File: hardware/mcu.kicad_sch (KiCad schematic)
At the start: 11 parts, among them J12 PICO UTIL, U1 Pico 2

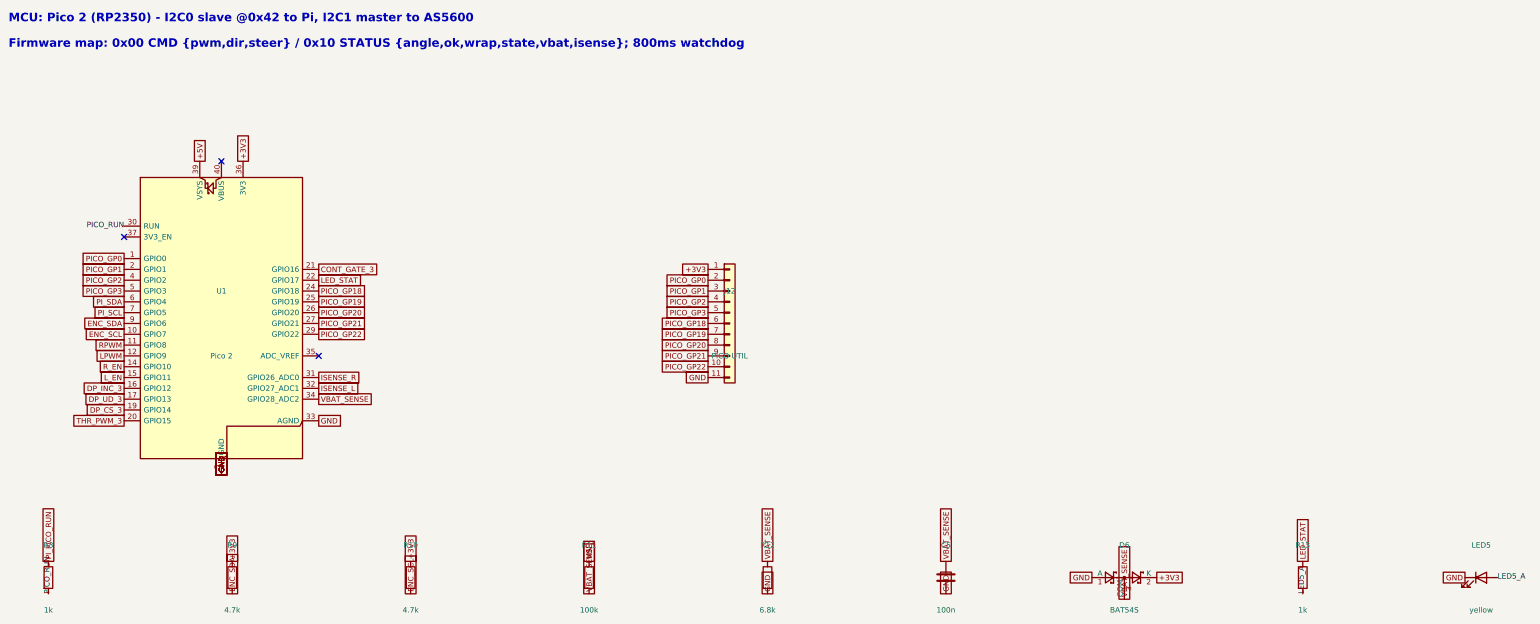
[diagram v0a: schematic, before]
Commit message: feat: custom footprints (Pololu buck, Pico+SWD), Pi-reflashable Pico via SWD on GPIO24/25
Co-Authored-By: Claude Fable 5 <noreply@anthropic.com>
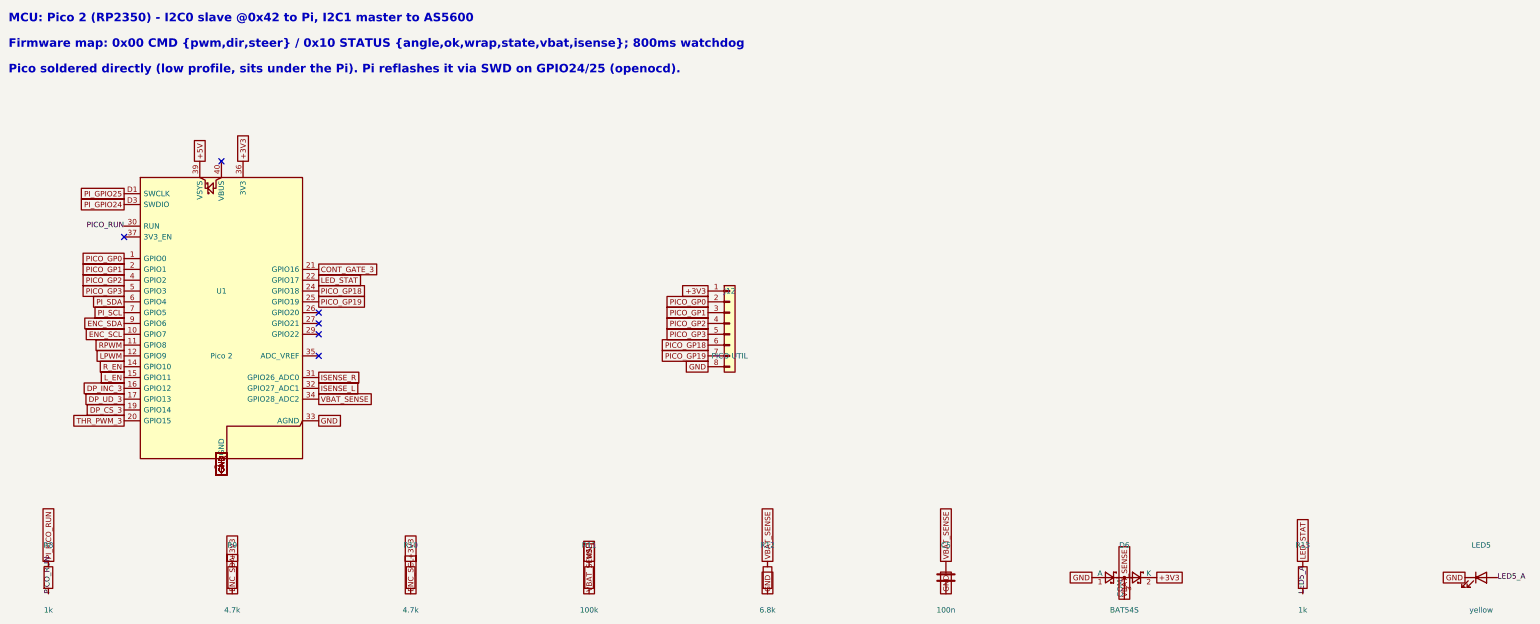
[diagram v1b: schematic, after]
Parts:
- J12: footprint Connector_PinHeader_2.54mm:PinHeader_1x11_P2.54mm_Vertical -> Connector_PinHeader_2.54mm:PinHeader_1x08_P2.54mm_Vertical; symbol Connector_Generic:Conn_01x11 -> Connector_Generic:Conn_01x08
- U1: footprint Module:RaspberryPi_Pico_Common_THT -> vanchor-helm:RaspberryPi_Pico_TH_SWD; symbol MCU_Module:RaspberryPi_Pico -> MCU_Module:RaspberryPi_Pico_Debug
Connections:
- net GND: now also J12.8 (Pin_8), U1.D2 (GND); no longer J12.11 (Pin_11)
- net PICO_GP20: no longer names the net of U1.26 (GPIO20)
- net PICO_GP20: no longer J12.8 (Pin_8)
- net PICO_GP21: no longer names the net of U1.27 (GPIO21)
- net PICO_GP21: no longer J12.9 (Pin_9)
- net PICO_GP22: no longer names the net of U1.29 (GPIO22)
- net PICO_GP22: no longer J12.10 (Pin_10)
- new net PI_GPIO24: U1.D3 (SWDIO)
- new net PI_GPIO25: U1.D1 (SWCLK)
- no-connect marks 3 -> 6
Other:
- note added: "Pico soldered directly (low profile, sits under the Pi). Pi reflashes it via SWD on GPIO24/25 (openocd)."
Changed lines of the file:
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@@
     (effects (font (size 2 2) (bold yes)) (justify left bottom))
   )
-  (symbol (lib_id "MCU_Module:RaspberryPi_Pico") (at 80.01 110.49 0) (unit 1)
+  (text "Pico soldered directly (low profile, sits under the Pi). Pi reflashes it via SWD on GPIO24/25 (openocd)." (exclude_from_sim no) (at 30 52 0)
+    (effects (font (size 2 2) (bold yes)) (justify left bottom))
+  )
+  (symbol (lib_id "MCU_Module:RaspberryPi_Pico_Debug") (at 80.01 110.49 0) (unit 1)
     (exclude_from_sim no) (in_bom yes) (on_board yes) (dnp no)
     (property "Reference" "U1" (at 80.01 102.87 0)
@@
     (property "Value" "Pico 2" (at 80.01 118.11 0)
       (effects (font (size 1.27 1.27))))
-    (property "Footprint" "Module:RaspberryPi_Pico_Common_THT" (at 80.01 110.49 0)
+    (property "Footprint" "vanchor-helm:RaspberryPi_Pico_TH_SWD" (at 80.01 110.49 0)
       (effects (font (size 1.27 1.27)) (hide yes)))
     (property "Datasheet" "" (at 80.01 110.49 0)
@@
     (pin "8")
     (pin "9")
+    (pin "D1")
+    (pin "D2")
+    (pin "D3")
     (instances (project "vanchor-helm" (path "/a0000000-0000-4000-8000-000000000001/c0000000-0000-4000-8000-000000000004" (reference "U1") (unit 1))))
   )
@@
     (instances (project "vanchor-helm" (path "/a0000000-0000-4000-8000-000000000001/c0000000-0000-4000-8000-000000000004" (reference "LED5") (unit 1))))
   )
-  (symbol (lib_id "Connector_Generic:Conn_01x11") (at 199.39 110.49 0) (unit 1)
+  (symbol (lib_id "Connector_Generic:Conn_01x08") (at 199.39 110.49 0) (unit 1)
     (exclude_from_sim no) (in_bom yes) (on_board yes) (dnp no)
     (property "Reference" "J12" (at 199.39 102.87 0)
@@
     (property "Value" "PICO UTIL" (at 199.39 118.11 0)
       (effects (font (size 1.27 1.27))))
-    (property "Footprint" "Connector_PinHeader_2.54mm:PinHeader_1x11_P2.54mm_Vertical" (at 199.39 110.49 0)
+    (property "Footprint" "Connector_PinHeader_2.54mm:PinHeader_1x08_P2.54mm_Vertical" (at 199.39 110.49 0)
       (effects (font (size 1.27 1.27)) (hide yes)))
     (property "Datasheet" "" (at 199.39 110.49 0)
       (effects (font (size 1.27 1.27)) (hide yes)))
     (pin "1")
-    (pin "10")
-    (pin "11")
     (pin "2")
     (pin "3")
@@
     (pin "7")
     (pin "8")
-    (pin "9")
     (instances (project "vanchor-helm" (path "/a0000000-0000-4000-8000-000000000001/c0000000-0000-4000-8000-000000000004" (reference "J12") (unit 1))))
   )
@@
       (effects (font (size 1.27 1.27)) (hide yes)))
   )
-  (global_label "PICO_GP20" (shape passive) (at 102.87 107.95 0.0) (fields_autoplaced yes)
-    (effects (font (size 1.27 1.27)) (justify left))
-    (property "Intersheetrefs" "${INTERSHEET_REFS}" (at 102.87 107.95 0)
-      (effects (font (size 1.27 1.27)) (hide yes)))
-  )
-  (global_label "PICO_GP21" (shape passive) (at 102.87 110.49 0.0) (fields_autoplaced yes)
-    (effects (font (size 1.27 1.27)) (justify left))
-    (property "Intersheetrefs" "${INTERSHEET_REFS}" (at 102.87 110.49 0)
-      (effects (font (size 1.27 1.27)) (hide yes)))
-  )
-  (global_label "GND" (shape passive) (at 80.01 146.05 270.0) (fields_autoplaced yes)
-    (effects (font (size 1.27 1.27)) (justify left))
-    (property "Intersheetrefs" "${INTERSHEET_REFS}" (at 80.01 146.05 0)
-      (effects (font (size 1.27 1.27)) (hide yes)))
-  )
-  (global_label "PICO_GP22" (shape passive) (at 102.87 113.03 0.0) (fields_autoplaced yes)
-    (effects (font (size 1.27 1.27)) (justify left))
-    (property "Intersheetrefs" "${INTERSHEET_REFS}" (at 102.87 113.03 0)
+  (global_label "GND" (shape passive) (at 80.01 146.05 270.0) (fields_autoplaced yes)
+    (effects (font (size 1.27 1.27)) (justify left))
+    (property "Intersheetrefs" "${INTERSHEET_REFS}" (at 80.01 146.05 0)
       (effects (font (size 1.27 1.27)) (hide yes)))
   )
@@
       (effects (font (size 1.27 1.27)) (hide yes)))
   )
+  (global_label "PI_GPIO25" (shape passive) (at 57.15 80.01 180.0) (fields_autoplaced yes)
+    (effects (font (size 1.27 1.27)) (justify right))
+    (property "Intersheetrefs" "${INTERSHEET_REFS}" (at 57.15 80.01 0)
+      (effects (font (size 1.27 1.27)) (hide yes)))
+  )
+  (global_label "GND" (shape passive) (at 80.01 146.05 270.0) (fields_autoplaced yes)
+    (effects (font (size 1.27 1.27)) (justify left))
+    (property "Intersheetrefs" "${INTERSHEET_REFS}" (at 80.01 146.05 0)
+      (effects (font (size 1.27 1.27)) (hide yes)))
+  )
+  (global_label "PI_GPIO24" (shape passive) (at 57.15 82.55 180.0) (fields_autoplaced yes)
+    (effects (font (size 1.27 1.27)) (justify right))
+    (property "Intersheetrefs" "${INTERSHEET_REFS}" (at 57.15 82.55 0)
+      (effects (font (size 1.27 1.27)) (hide yes)))
+  )
   (global_label "PI_PICO_RUN" (shape passive) (at 39.37 166.37 90.0) (fields_autoplaced yes)
     (effects (font (size 1.27 1.27)) (justify left))
@@
       (effects (font (size 1.27 1.27)) (hide yes)))
   )
-  (global_label "+3V3" (shape passive) (at 194.31 97.79 180.0) (fields_autoplaced yes)
-    (effects (font (size 1.27 1.27)) (justify right))
-    (property "Intersheetrefs" "${INTERSHEET_REFS}" (at 194.31 97.79 0)
-      (effects (font (size 1.27 1.27)) (hide yes)))
-  )
-  (global_label "PICO_GP0" (shape passive) (at 194.31 100.33 180.0) (fields_autoplaced yes)
-    (effects (font (size 1.27 1.27)) (justify right))
-    (property "Intersheetrefs" "${INTERSHEET_REFS}" (at 194.31 100.33 0)
-      (effects (font (size 1.27 1.27)) (hide yes)))
-  )
-  (global_label "PICO_GP1" (shape passive) (at 194.31 102.87 180.0) (fields_autoplaced yes)
+  (global_label "+3V3" (shape passive) (at 194.31 102.87 180.0) (fields_autoplaced yes)
     (effects (font (size 1.27 1.27)) (justify right))
     (property "Intersheetrefs" "${INTERSHEET_REFS}" (at 194.31 102.87 0)
       (effects (font (size 1.27 1.27)) (hide yes)))
   )
-  (global_label "PICO_GP2" (shape passive) (at 194.31 105.41 180.0) (fields_autoplaced yes)
+  (global_label "PICO_GP0" (shape passive) (at 194.31 105.41 180.0) (fields_autoplaced yes)
     (effects (font (size 1.27 1.27)) (justify right))
     (property "Intersheetrefs" "${INTERSHEET_REFS}" (at 194.31 105.41 0)
       (effects (font (size 1.27 1.27)) (hide yes)))
   )
-  (global_label "PICO_GP3" (shape passive) (at 194.31 107.95 180.0) (fields_autoplaced yes)
+  (global_label "PICO_GP1" (shape passive) (at 194.31 107.95 180.0) (fields_autoplaced yes)
     (effects (font (size 1.27 1.27)) (justify right))
     (property "Intersheetrefs" "${INTERSHEET_REFS}" (at 194.31 107.95 0)
       (effects (font (size 1.27 1.27)) (hide yes)))
   )
-  (global_label "PICO_GP18" (shape passive) (at 194.31 110.49 180.0) (fields_autoplaced yes)
+  (global_label "PICO_GP2" (shape passive) (at 194.31 110.49 180.0) (fields_autoplaced yes)
     (effects (font (size 1.27 1.27)) (justify right))
     (property "Intersheetrefs" "${INTERSHEET_REFS}" (at 194.31 110.49 0)
       (effects (font (size 1.27 1.27)) (hide yes)))
   )
-  (global_label "PICO_GP19" (shape passive) (at 194.31 113.03 180.0) (fields_autoplaced yes)
+  (global_label "PICO_GP3" (shape passive) (at 194.31 113.03 180.0) (fields_autoplaced yes)
     (effects (font (size 1.27 1.27)) (justify right))
     (property "Intersheetrefs" "${INTERSHEET_REFS}" (at 194.31 113.03 0)
       (effects (font (size 1.27 1.27)) (hide yes)))
   )
-  (global_label "PICO_GP20" (shape passive) (at 194.31 115.57 180.0) (fields_autoplaced yes)
+  (global_label "PICO_GP18" (shape passive) (at 194.31 115.57 180.0) (fields_autoplaced yes)
     (effects (font (size 1.27 1.27)) (justify right))
     (property "Intersheetrefs" "${INTERSHEET_REFS}" (at 194.31 115.57 0)
       (effects (font (size 1.27 1.27)) (hide yes)))
   )
-  (global_label "PICO_GP21" (shape passive) (at 194.31 118.11 180.0) (fields_autoplaced yes)
+  (global_label "PICO_GP19" (shape passive) (at 194.31 118.11 180.0) (fields_autoplaced yes)
     (effects (font (size 1.27 1.27)) (justify right))
     (property "Intersheetrefs" "${INTERSHEET_REFS}" (at 194.31 118.11 0)
       (effects (font (size 1.27 1.27)) (hide yes)))
   )
-  (global_label "PICO_GP22" (shape passive) (at 194.31 120.65 180.0) (fields_autoplaced yes)
+  (global_label "GND" (shape passive) (at 194.31 120.65 180.0) (fields_autoplaced yes)
     (effects (font (size 1.27 1.27)) (justify right))
     (property "Intersheetrefs" "${INTERSHEET_REFS}" (at 194.31 120.65 0)
       (effects (font (size 1.27 1.27)) (hide yes)))
   )
-  (global_label "GND" (shape passive) (at 194.31 123.19 180.0) (fields_autoplaced yes)
-    (effects (font (size 1.27 1.27)) (justify right))
-    (property "Intersheetrefs" "${INTERSHEET_REFS}" (at 194.31 123.19 0)
-      (effects (font (size 1.27 1.27)) (hide yes)))
-  )
+  (no_connect (at 102.87 107.95))
+  (no_connect (at 102.87 110.49))
+  (no_connect (at 102.87 113.03))
   (no_connect (at 102.87 118.11))
   (no_connect (at 57.15 90.17))

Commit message: feat: MPN table merged into schematic fields; SES import script
Co-Authored-By: Claude Fable 5 <noreply@anthropic.com>
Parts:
- D6: MPN (none) -> BAT54S,215
- U1: MPN (none) -> Raspberry Pi Pico 2 (SC1632)
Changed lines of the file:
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@@
     (property "Datasheet" "" (at 80.01 110.49 0)
+      (effects (font (size 1.27 1.27)) (hide yes)))
+    (property "MPN" "Raspberry Pi Pico 2 (SC1632)" (at 80.01 110.49 0)
       (effects (font (size 1.27 1.27)) (hide yes)))
     (pin "1")
@@
     (property "Datasheet" "" (at 292.1 170.18 0)
       (effects (font (size 1.27 1.27)) (hide yes)))
+    (property "MPN" "BAT54S,215" (at 292.1 170.18 0)
+      (effects (font (size 1.27 1.27)) (hide yes)))
     (pin "1")

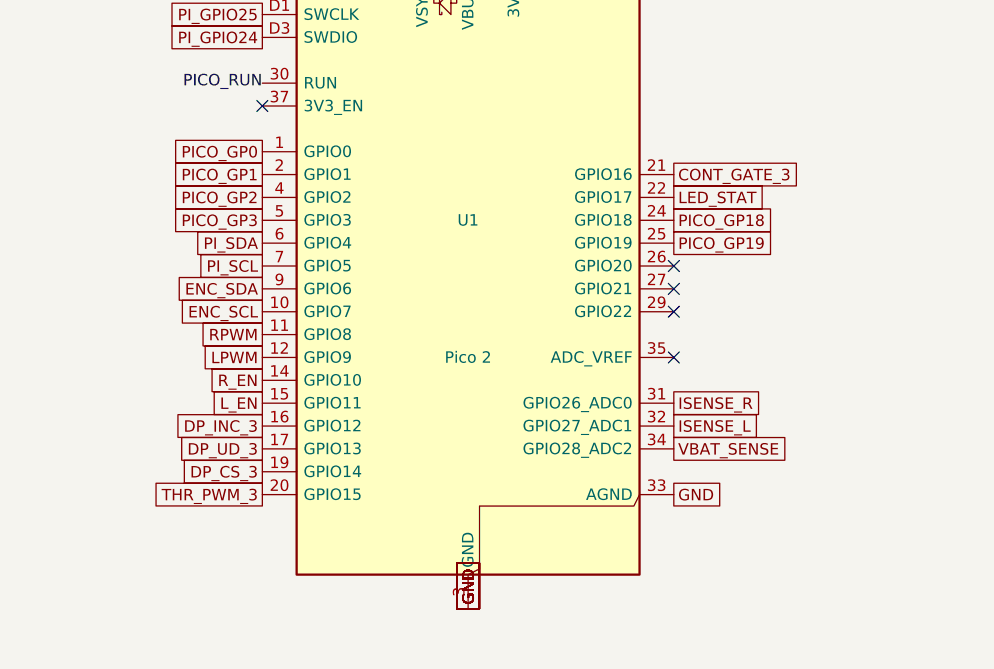
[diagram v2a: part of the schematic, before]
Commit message: feat: on-board 800W H-bridge (HIP4082 + 8 FET, ACS758, M5 lugs) + BTN8982 servo bridge; 160x120 board, placement DRC-clean
Co-Authored-By: Claude Fable 5 <noreply@anthropic.com>
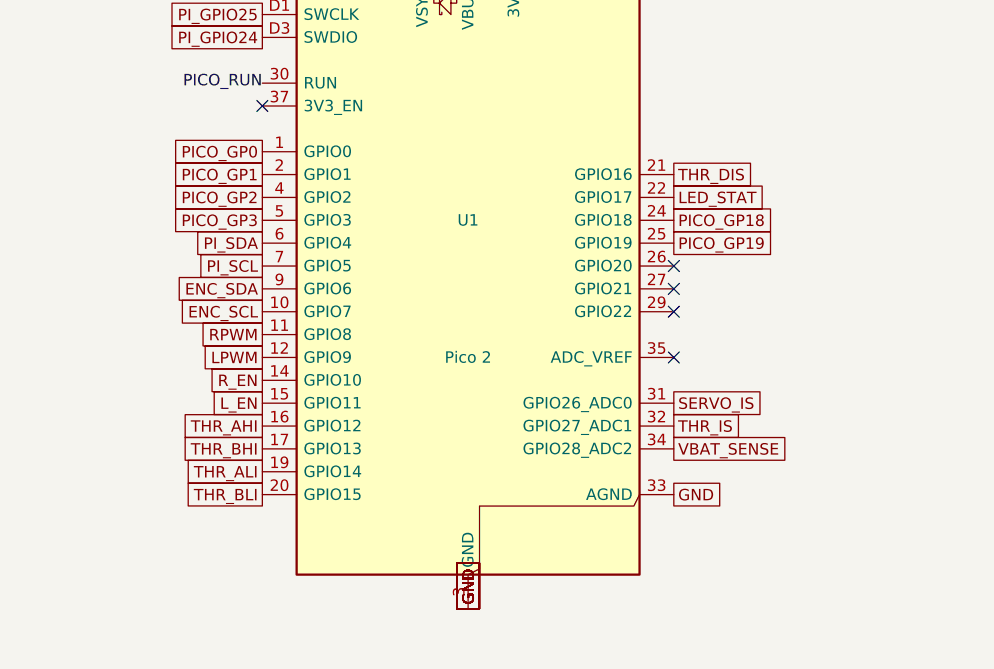
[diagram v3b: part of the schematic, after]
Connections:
- net CONT_GATE_3 renamed THR_DIS
- net DP_CS_3 renamed THR_ALI
- net DP_INC_3 renamed THR_AHI
- net DP_UD_3 renamed THR_BHI
- net ISENSE_L renamed THR_IS
- net ISENSE_R renamed SERVO_IS
- net THR_PWM_3 renamed THR_BLI
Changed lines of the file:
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@@
       (effects (font (size 1.27 1.27)) (hide yes)))
   )
-  (global_label "DP_INC_3" (shape passive) (at 57.15 125.73 180.0) (fields_autoplaced yes)
+  (global_label "THR_AHI" (shape passive) (at 57.15 125.73 180.0) (fields_autoplaced yes)
     (effects (font (size 1.27 1.27)) (justify right))
     (property "Intersheetrefs" "${INTERSHEET_REFS}" (at 57.15 125.73 0)
       (effects (font (size 1.27 1.27)) (hide yes)))
   )
-  (global_label "DP_UD_3" (shape passive) (at 57.15 128.27 180.0) (fields_autoplaced yes)
+  (global_label "THR_BHI" (shape passive) (at 57.15 128.27 180.0) (fields_autoplaced yes)
     (effects (font (size 1.27 1.27)) (justify right))
     (property "Intersheetrefs" "${INTERSHEET_REFS}" (at 57.15 128.27 0)
@@
       (effects (font (size 1.27 1.27)) (hide yes)))
   )
-  (global_label "DP_CS_3" (shape passive) (at 57.15 130.81 180.0) (fields_autoplaced yes)
+  (global_label "THR_ALI" (shape passive) (at 57.15 130.81 180.0) (fields_autoplaced yes)
     (effects (font (size 1.27 1.27)) (justify right))
     (property "Intersheetrefs" "${INTERSHEET_REFS}" (at 57.15 130.81 0)
       (effects (font (size 1.27 1.27)) (hide yes)))
   )
-  (global_label "THR_PWM_3" (shape passive) (at 57.15 133.35 180.0) (fields_autoplaced yes)
+  (global_label "THR_BLI" (shape passive) (at 57.15 133.35 180.0) (fields_autoplaced yes)
     (effects (font (size 1.27 1.27)) (justify right))
     (property "Intersheetrefs" "${INTERSHEET_REFS}" (at 57.15 133.35 0)
       (effects (font (size 1.27 1.27)) (hide yes)))
   )
-  (global_label "CONT_GATE_3" (shape passive) (at 102.87 97.79 0.0) (fields_autoplaced yes)
+  (global_label "THR_DIS" (shape passive) (at 102.87 97.79 0.0) (fields_autoplaced yes)
     (effects (font (size 1.27 1.27)) (justify left))
     (property "Intersheetrefs" "${INTERSHEET_REFS}" (at 102.87 97.79 0)
@@
     (effects (font (size 1.27 1.27)) (justify right))
   )
-  (global_label "ISENSE_R" (shape passive) (at 102.87 123.19 0.0) (fields_autoplaced yes)
+  (global_label "SERVO_IS" (shape passive) (at 102.87 123.19 0.0) (fields_autoplaced yes)
     (effects (font (size 1.27 1.27)) (justify left))
     (property "Intersheetrefs" "${INTERSHEET_REFS}" (at 102.87 123.19 0)
       (effects (font (size 1.27 1.27)) (hide yes)))
   )
-  (global_label "ISENSE_L" (shape passive) (at 102.87 125.73 0.0) (fields_autoplaced yes)
+  (global_label "THR_IS" (shape passive) (at 102.87 125.73 0.0) (fields_autoplaced yes)
     (effects (font (size 1.27 1.27)) (justify left))
     (property "Intersheetrefs" "${INTERSHEET_REFS}" (at 102.87 125.73 0)
